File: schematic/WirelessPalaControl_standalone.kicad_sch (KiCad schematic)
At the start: 25 parts, among them J1 6P4C, J2 MCU UART, J3 WeMos_mini_Hat_Left, J4 WeMos_mini_Hat_Right, Q1 AO3400A, Q2 AO3400A, U1 AMS1117-3.3

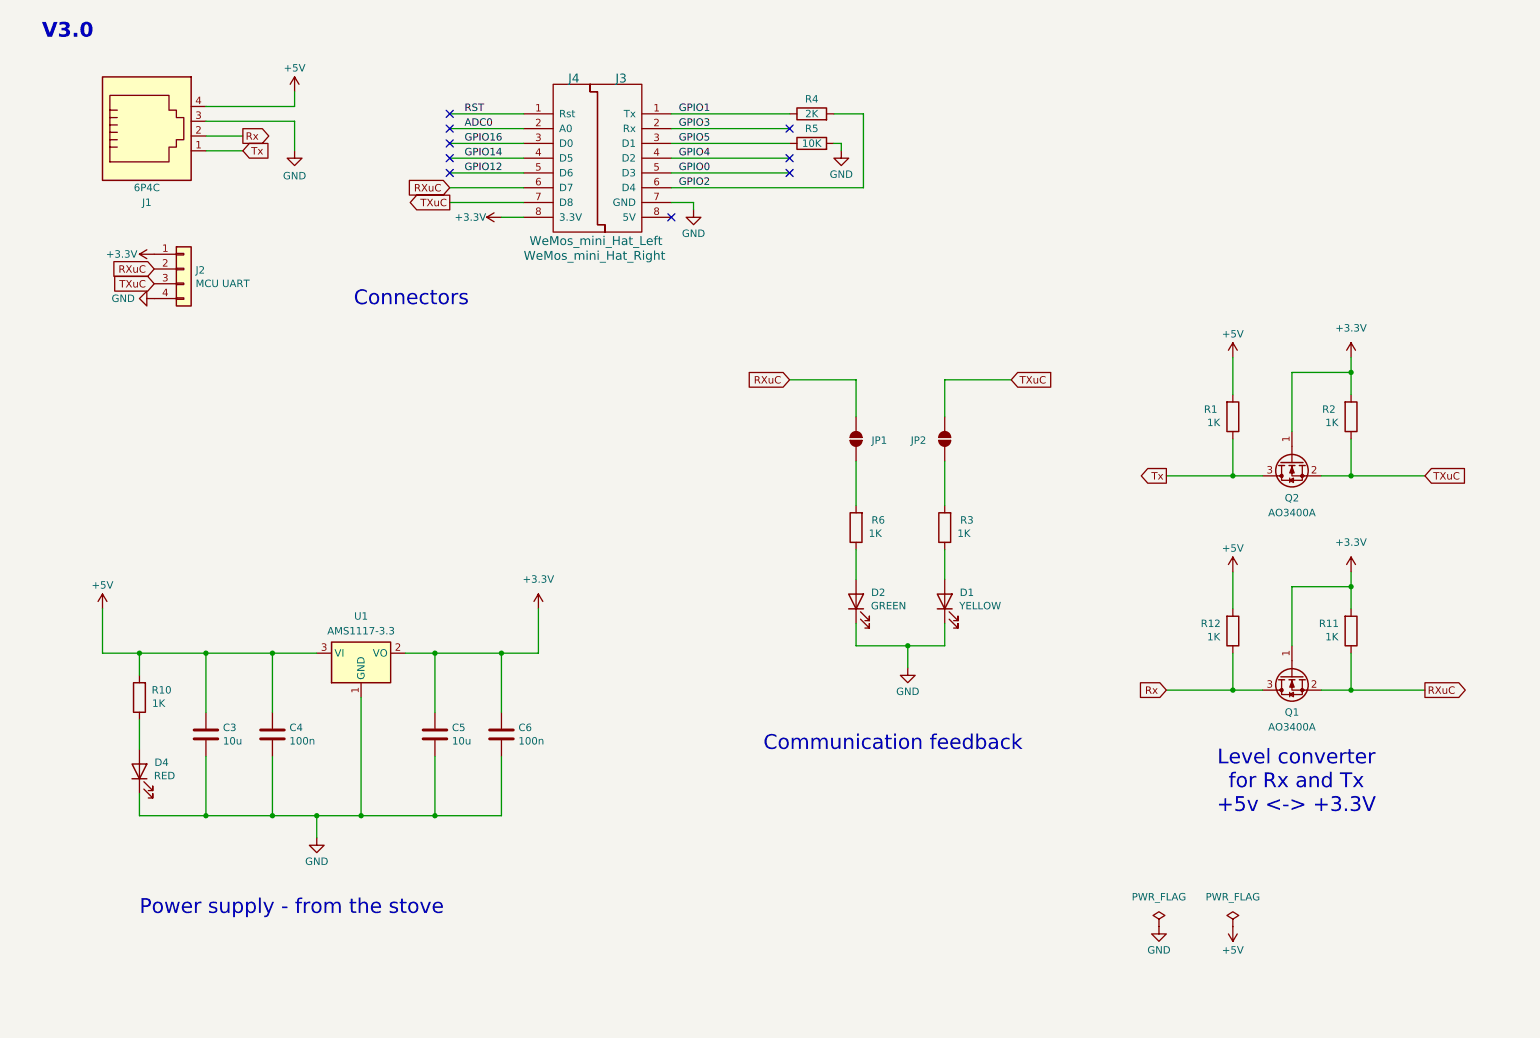
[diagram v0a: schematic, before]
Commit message: feat(hw): Redesign standalone version with optionnal LED activation
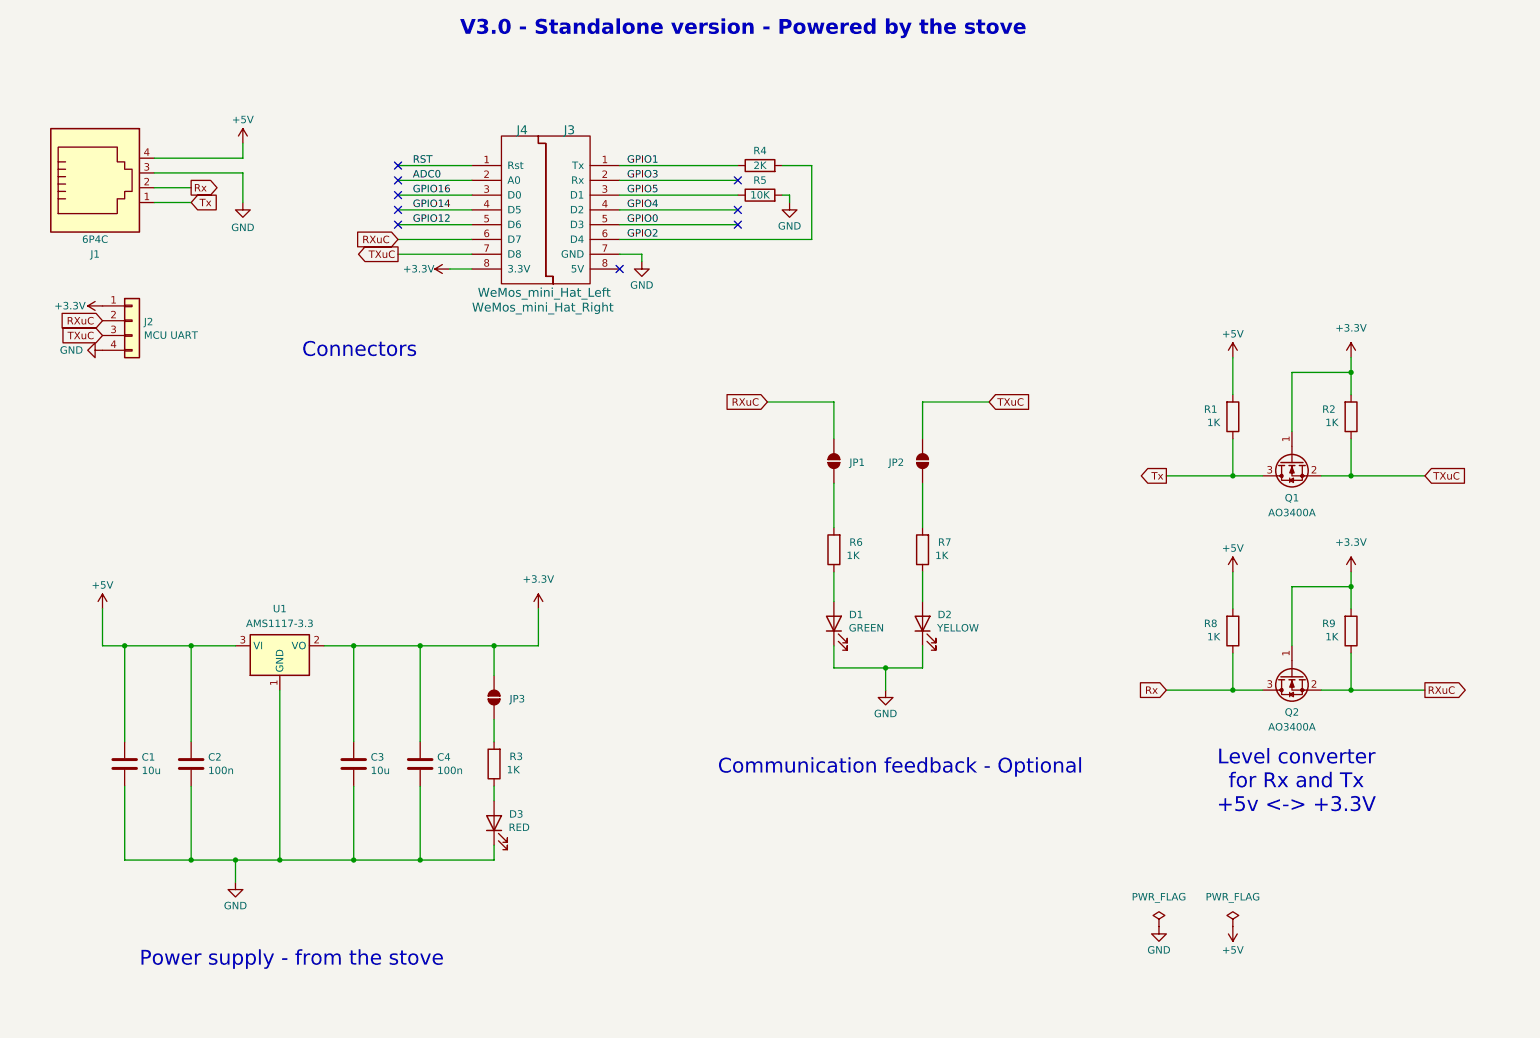
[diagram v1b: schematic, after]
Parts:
- added JP3: SolderJumper_2_Open, Jumper:SolderJumper-2_P1.3mm_Open_TrianglePad1.0x1.5mm, symbol Jumper:SolderJumper_2_Open
- renumbered C3 to C1, C4 to C2, C5 to C3, C6 to C4, D2 to D1, D1 to D2, D4 to D3, Q2 to Q1, Q1 to Q2, R10 to R3, R3 to R7, R12 to R8, R11 to R9
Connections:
- net +3.3V: now also JP3.1 (A)
- net +5V: no longer R3.2
- new net: JP3.2 (B), R3.2
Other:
- note added: "Communication feedback - Optional"
- note added: "V3.0 - Standalone version - Powered by the stove"
- note removed: "Communication feedback"
- note removed: "V3.0"
- moved on the sheet: C1, C2, C3, C4, D1, D2, D3, J1, J2, J3, J4, JP1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

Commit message: feat(hw): Add connector to directly solder a RJ11 cable
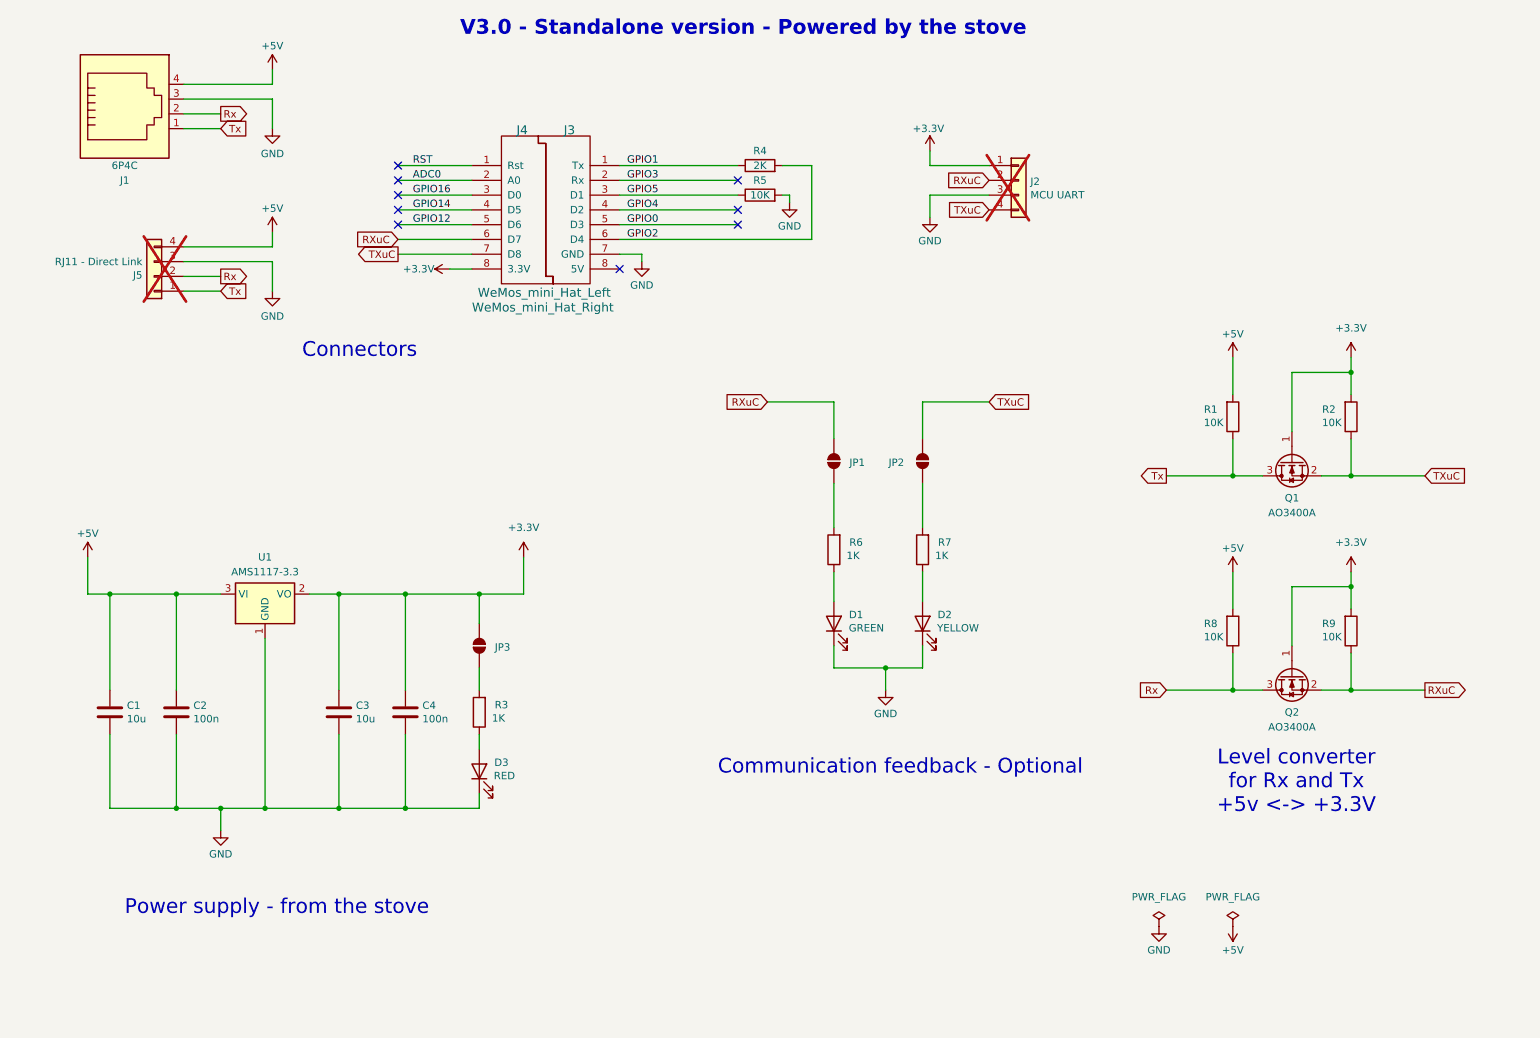
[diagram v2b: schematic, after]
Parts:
- added J5: RJ11 - Direct Link, Connector_PinHeader_2.54mm:PinHeader_1x04_P2.54mm_Vertical, symbol Connector_Generic:Conn_01x04
- J2: now not fitted
- R1, R2, R8, R9: value 1K -> 10K
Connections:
- net +5V: now also J5.4 (Pin_4)
- net GND: now also J2.3 (Pin_3), J5.3 (Pin_3); no longer J2.4 (Pin_4)
- net Rx: now also J5.2 (Pin_2)
- net TXuC: now also J2.4 (Pin_4); no longer J2.3 (Pin_3)
- net Tx: now also J5.1 (Pin_1)
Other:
- moved on the sheet: C1, C2, C3, C4, D3, J1, JP3, R3, U1

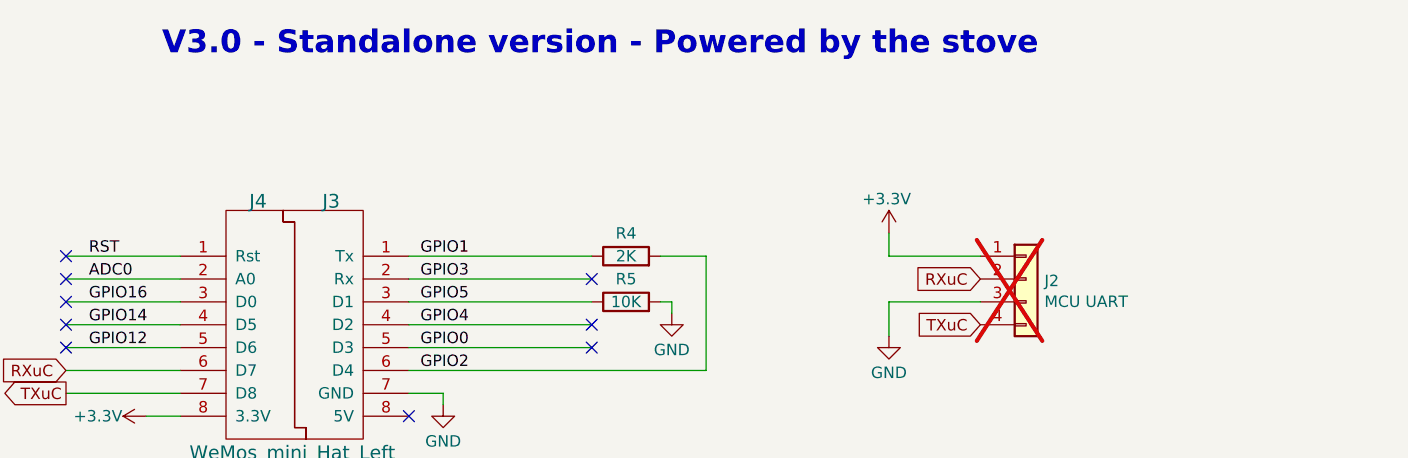
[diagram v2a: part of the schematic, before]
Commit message: feat(hw): Update BOM with JLCPCB part numbers
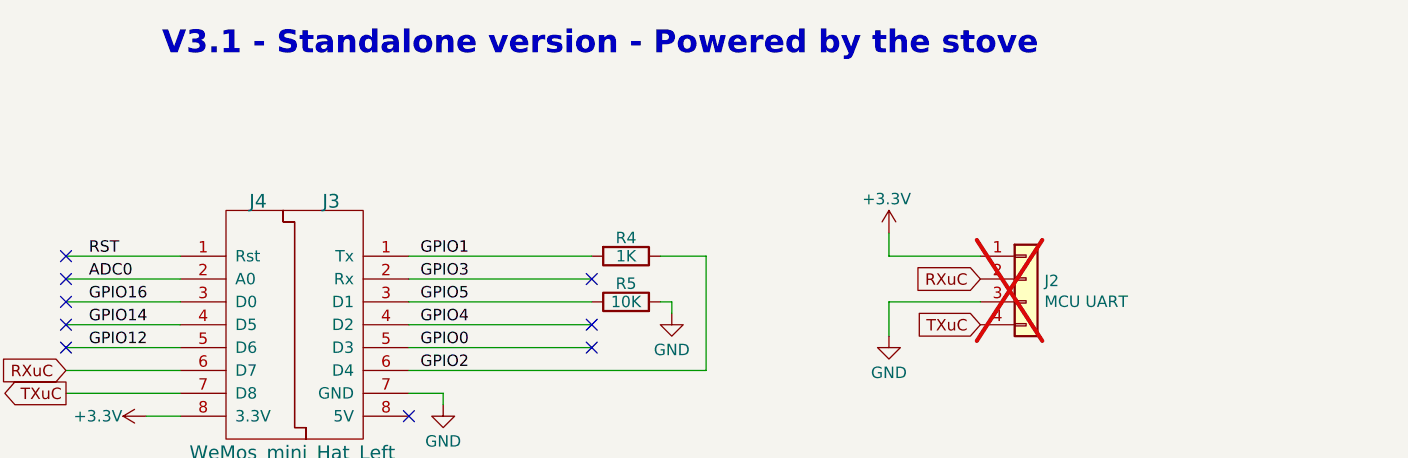
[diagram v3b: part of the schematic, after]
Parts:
- C1, C3: LCSC C49678 -> C440198
- D1: LCSC C84256 -> C2297
- D2: LCSC C84256 -> C2296
- J3, J4: now left out of the parts list
- R1, R2, R8, R9: LCSC C17513 -> C17414
- R4: value 2K -> 1K; LCSC C17604 -> C17513
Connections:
- net GPIO1: now also R4.2; no longer R4.1
- net GPIO2: now also R4.1; no longer R4.2
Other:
- note added: "V3.1 - Standalone version - Powered by the stove"
- note removed: "V3.0 - Standalone version - Powered by the stove"
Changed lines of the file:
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@@
 	(generator_version "9.0")
 	(paper "A4")
-	(text "V3.0 - Standalone version - Powered by the stove"
+	(text "V3.1 - Standalone version - Powered by the stove"
 		(exclude_from_sim no)
 		(at 94.488 21.082 0)
@@
 		(dnp no)
 		(property "Reference" "R5"
-			(at 146.05 45.72 90)
+			(at 146.05 46.228 90)
 			(effects
 				(font
@@
 	)
 	(symbol
+		(lib_id "Device:R")
+		(at 146.05 43.18 270)
+		(unit 1)
+		(exclude_from_sim no)
+		(in_bom yes)
+		(on_board yes)
+		(dnp no)
+		(property "Reference" "R4"
+			(at 146.05 41.148 90)
+			(effects
+				(font
+					(size 1.27 1.27)
+				)
+			)
+		)
+		(property "Value" "1K"
+			(at 146.05 43.18 90)
+			(effects
+				(font
+					(size 1.27 1.27)
+				)
+			)
+		)
+		(property "Footprint" "Resistor_SMD:R_0805_2012Metric_Pad1.20x1.40mm_HandSolder"
+			(at 146.05 41.402 90)
+			(effects
+				(font
+					(size 1.27 1.27)
+				)
+				(hide yes)
+			)
+		)
+		(property "Datasheet" "~"
+			(at 146.05 43.18 0)
+			(effects
+				(font
+					(size 1.27 1.27)
+				)
+				(hide yes)
+			)
+		)
+		(property "Description" ""
+			(at 146.05 43.18 0)
+			(effects
+				(font
+					(size 1.27 1.27)
+				)
+				(hide yes)
+			)
+		)
+		(property "LCSC" "C17513"
+			(at 146.05 43.18 90)
+			(effects
+				(font
+					(size 1.27 1.27)
+				)
+				(hide yes)
+			)
+		)
+		(pin "1"
+		)
+		(pin "2"
+		)
+		(instances
+			(project "WirelessPalaControl_standalone"
+				(path "/7b732a5c-181e-4123-b888-9221491b7bcc"
+					(reference "R4")
+					(unit 1)
+				)
+			)
+		)
+	)
+	(symbol
 		(lib_id "power:VDD")
 		(at 30.48 110.49 0)
@@
 			)
 		)
-		(property "LCSC" "C17513"
+		(property "LCSC" "C17414"
 			(at 247.65 86.36 90)
 			(effects
@@
 		(unit 1)
 		(exclude_from_sim no)
-		(in_bom yes)
+		(in_bom no)
 		(on_board yes)
 		(dnp no)
@@
 			)
 		)
-		(property "LCSC" "C49678"
+		(property "LCSC" "C440198"
 			(at 73.66 137.16 0)
 			(effects
@@
 			)
 		)
-		(property "LCSC" "C84256"
+		(property "LCSC" "C2297"
 			(at 158.75 121.92 0)
 			(effects
@@
 		(unit 1)
 		(exclude_from_sim no)
-		(in_bom yes)
+		(in_bom no)
 		(on_board yes)
 		(dnp no)
@@
 			)
 		)
-		(property "LCSC" "C49678"
+		(property "LCSC" "C440198"
 			(at 34.29 137.16 0)
 			(effects
@@
 			)
 		)
-		(property "LCSC" "C84256"
+		(property "LCSC" "C2296"
 			(at 173.99 121.92 0)
 			(effects
@@
 			)
 		)
-		(property "LCSC" "C17513"
+		(property "LCSC" "C17414"
 			(at 227.33 123.19 90)
 			(effects
@@
 			)
 		)
-		(property "LCSC" "C17513"
+		(property "LCSC" "C17414"
 			(at 227.33 86.36 90)
 			(effects
@@
 			)
 		)
-		(property "LCSC" "C17513"
+		(property "LCSC" "C17414"
 			(at 247.65 123.19 90)
 			(effects
@@
 					(unit 1)
 				)
-			)
-		)
-	)
-	(symbol
-		(lib_id "Device:R")
-		(at 146.05 43.18 90)
-		(unit 1)
-		(exclude_from_sim no)
-		(in_bom yes)
-		(on_board yes)
-		(dnp no)
-		(property "Reference" "R4"
-			(at 146.05 40.64 90)
-			(effects
-				(font
-					(size 1.27 1.27)
-				)
-			)
-		)
-		(property "Value" "2K"
-			(at 146.05 43.18 90)
-			(effects
-				(font
-					(size 1.27 1.27)
-				)
-			)
-		)
-		(property "Footprint" "Resistor_SMD:R_0805_2012Metric_Pad1.20x1.40mm_HandSolder"
-			(at 146.05 44.958 90)
-			(effects
-				(font
-					(size 1.27 1.27)
-				)
-				(hide yes)
-			)
-		)
-		(property "Datasheet" "~"
-			(at 146.05 43.18 0)
-			(effects
-				(font
-					(size 1.27 1.27)
-				)
-				(hide yes)
-			)
-		)
-		(property "Description" ""
-			(at 146.05 43.18 0)
-			(effects
-				(font
-					(size 1.27 1.27)
-				)
-				(hide yes)
-			)
-		)
-		(property "LCSC" "C17604"
-			(at 146.05 43.18 90)
-			(effects
-				(font
-					(size 1.27 1.27)
-				)
-				(hide yes)
-			)
-		)
-		(pin "1"
-		)
-		(pin "2"
-		)
-		(instances
-			(project "WirelessPalaControl"
-				(path "/7b732a5c-181e-4123-b888-9221491b7bcc"
-					(reference "R4")
-					(unit 1)
-				)
